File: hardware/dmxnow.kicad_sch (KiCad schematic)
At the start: 62 parts, among them J1 WAGO 2604-1102 (L N in), J2 DMX tail (1 GND 2 B 3 A), J3 PROG (3V3 GND D- D+ EN BOOT), J4 WAGO 2604-1102 (L_SW N out 1), J5 WAGO 2604-1102 (VLED_IN GND_L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, J6 WAGO 2604-1105 (VLED CH1-CH4), J7 WAGO 2604-1102 (L_SW N out 2,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, K1 G5RL-1A-E-HR DC5, Q1 AO3400A, Q2 AOD2610E, Q3 AOD2610E, Q4 AOD2610E, Q5 AOD2610E, SW1 PTS810 (BOOT/maintenance), U1 ESP32-C3-MINI-1-N4, U2 SP3485EN, U3 AP2112K-3.3, U4 74AHCT125

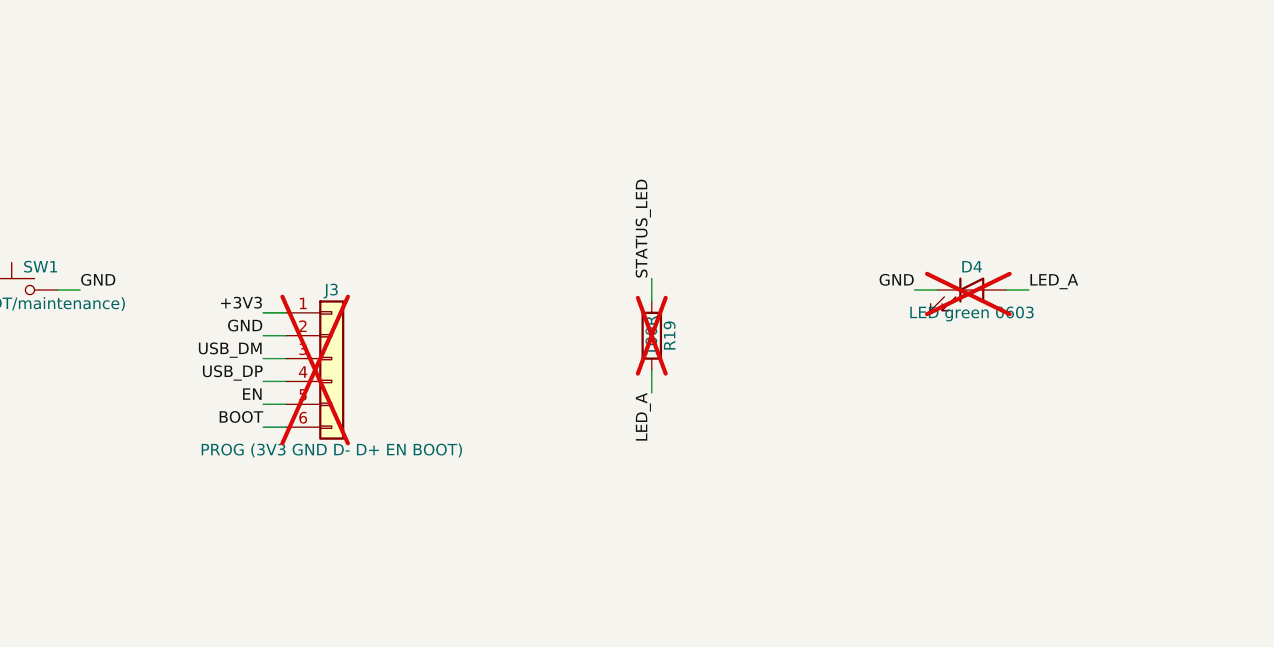
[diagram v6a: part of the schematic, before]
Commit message: hardware: cinquième passe de revue (J3 +5V, LED rouge, R15-R18, notes de commande)
- J3 passe à 7 pastilles : +5V (entrée de U3) pour programmer hors secteur sans
  réalimenter la sortie de l'AP2112K ; marquages 3V3 / 5V
- D4 LED rouge KT-0603R (C2286) + R19 330R : une LED verte VF 3,1 V ne s'allume pas
- R15-R18 décalées de 0,5 mm (4 mm sans composant de chaque côté de la découpe)
- marquages J2 en 1,0 mm ; références F1 / F2 ramenées sur la carte
- vias d'îlot : anneau entier dans les deux plans (plus de via à cheval sur un bord)
- SPEC : courant TX 350 mA, question J3-3V3 close, risque R-16 (OVP IRM-03 / AP2112K)
- README / REVIEW : 2 designs chez JLCPCB, remarque de commande complète, J6 arrêté chez WAGO

Co-Authored-By: Claude Opus 5.5 <noreply@anthropic.com>
Claude-Session: https://claude.ai/code/session_01B51M6ZY5abLxTmcevvc8Le
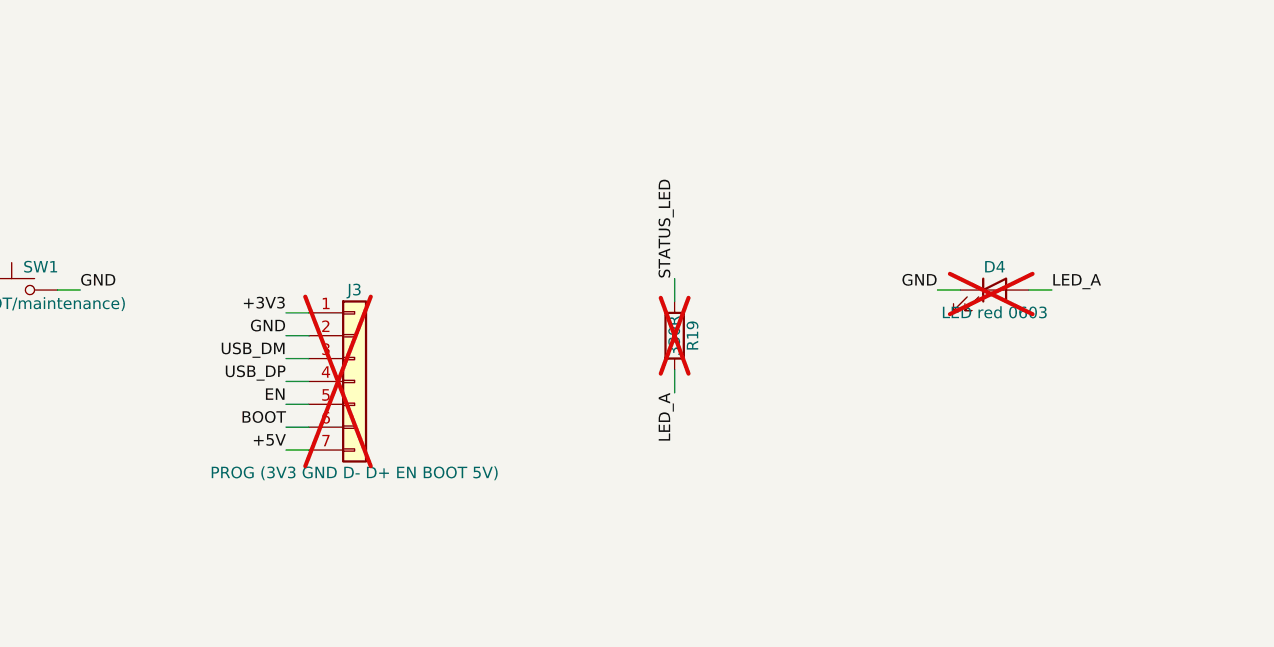
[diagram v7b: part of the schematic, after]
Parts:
- D4: value LED green 0603 -> LED red 0603; LCSC C12624 -> C2286; MPN KT-0603G -> KT-0603R
- J3: value PROG (3V3 GND D- D+ EN BOOT) -> PROG (3V3 GND D- D+ EN BOOT 5V); footprint Connector_PinHeader_2.54mm:PinHeader_1x06_P2.54mm_Vertical -> Connector_PinHeader_2.54mm:PinHeader_1x07_P2.54mm_Vertical; symbol Connector_Generic:Conn_01x06 -> Connector_Generic:Conn_01x07
- R19: value 100R -> 330R; LCSC C22775 -> C23138
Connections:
- net +5V: now also J3.7 (Pin_7)
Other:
- moved on the sheet: D4, R19
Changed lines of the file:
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@@
   )
   (symbol
-    (lib_id "Connector_Generic:Conn_01x06")
-    (at 325.12 147.32 0)
+    (lib_id "Connector_Generic:Conn_01x07")
+    (at 327.66 149.86 0)
     (unit 1)
     (in_bom yes)
@@
     (dnp yes)
     (property "Reference" "J3"
-      (at 325.12 139.7 0)
+      (at 327.66 139.7 0)
       (id 0)
       (effects
@@
       )
     )
-    (property "Value" "PROG (3V3 GND D- D+ EN BOOT)"
-      (at 325.12 157.48 0)
+    (property "Value" "PROG (3V3 GND D- D+ EN BOOT 5V)"
+      (at 327.66 160.02 0)
       (id 1)
       (effects
@@
       )
     )
-    (property "Footprint" "Connector_PinHeader_2.54mm:PinHeader_1x06_P2.54mm_Vertical"
-      (at 325.12 147.32 0)
+    (property "Footprint" "Connector_PinHeader_2.54mm:PinHeader_1x07_P2.54mm_Vertical"
+      (at 327.66 149.86 0)
       (id 2)
       (effects
@@
     )
     (property "Datasheet" ""
-      (at 325.12 147.32 0)
+      (at 327.66 149.86 0)
       (id 3)
       (effects
@@
     )
     (property "MPN" ""
-      (at 325.12 147.32 0)
+      (at 327.66 149.86 0)
       (id 4)
       (effects
@@
     )
     (property "LCSC" ""
-      (at 325.12 147.32 0)
+      (at 327.66 149.86 0)
       (id 5)
       (effects
@@
     )
     (property "Section" "main"
-      (at 325.12 147.32 0)
+      (at 327.66 149.86 0)
       (id 6)
       (effects
@@
     )
     (pin "6"
+    )
+    (pin "7"
     )
     (instances
@@
   (wire
     (pts
+      (xy 322.58 142.24)
       (xy 320.04 142.24)
-      (xy 317.5 142.24)
     )
     (stroke
@@
   )
   (label "+3V3"
-    (at 317.5 142.24 180)
-    (fields_autoplaced)
-    (effects
-      (font
-        (size 1.27 1.27)
-      )
-      (justify right bottom)
-    )
-  )
-  (wire
-    (pts
+    (at 320.04 142.24 180)
+    (fields_autoplaced)
+    (effects
+      (font
+        (size 1.27 1.27)
+      )
+      (justify right bottom)
+    )
+  )
+  (wire
+    (pts
+      (xy 322.58 144.78)
       (xy 320.04 144.78)
-      (xy 317.5 144.78)
     )
     (stroke
@@
   )
   (label "GND"
-    (at 317.5 144.78 180)
-    (fields_autoplaced)
-    (effects
-      (font
-        (size 1.27 1.27)
-      )
-      (justify right bottom)
-    )
-  )
-  (wire
-    (pts
+    (at 320.04 144.78 180)
+    (fields_autoplaced)
+    (effects
+      (font
+        (size 1.27 1.27)
+      )
+      (justify right bottom)
+    )
+  )
+  (wire
+    (pts
+      (xy 322.58 147.32)
       (xy 320.04 147.32)
-      (xy 317.5 147.32)
     )
     (stroke
@@
   )
   (label "USB_DM"
-    (at 317.5 147.32 180)
-    (fields_autoplaced)
-    (effects
-      (font
-        (size 1.27 1.27)
-      )
-      (justify right bottom)
-    )
-  )
-  (wire
-    (pts
+    (at 320.04 147.32 180)
+    (fields_autoplaced)
+    (effects
+      (font
+        (size 1.27 1.27)
+      )
+      (justify right bottom)
+    )
+  )
+  (wire
+    (pts
+      (xy 322.58 149.86)
       (xy 320.04 149.86)
-      (xy 317.5 149.86)
     )
     (stroke
@@
   )
   (label "USB_DP"
-    (at 317.5 149.86 180)
-    (fields_autoplaced)
-    (effects
-      (font
-        (size 1.27 1.27)
-      )
-      (justify right bottom)
-    )
-  )
-  (wire
-    (pts
+    (at 320.04 149.86 180)
+    (fields_autoplaced)
+    (effects
+      (font
+        (size 1.27 1.27)
+      )
+      (justify right bottom)
+    )
+  )
+  (wire
+    (pts
+      (xy 322.58 152.4)
       (xy 320.04 152.4)
-      (xy 317.5 152.4)
     )
     (stroke
@@
   )
   (label "EN"
-    (at 317.5 152.4 180)
-    (fields_autoplaced)
-    (effects
-      (font
-        (size 1.27 1.27)
-      )
-      (justify right bottom)
-    )
-  )
-  (wire
-    (pts
+    (at 320.04 152.4 180)
+    (fields_autoplaced)
+    (effects
+      (font
+        (size 1.27 1.27)
+      )
+      (justify right bottom)
+    )
+  )
+  (wire
+    (pts
+      (xy 322.58 154.94)
       (xy 320.04 154.94)
-      (xy 317.5 154.94)
     )
     (stroke
@@
   )
   (label "BOOT"
-    (at 317.5 154.94 180)
+    (at 320.04 154.94 180)
+    (fields_autoplaced)
+    (effects
+      (font
+        (size 1.27 1.27)
+      )
+      (justify right bottom)
+    )
+  )
+  (wire
+    (pts
+      (xy 322.58 157.48)
+      (xy 320.04 157.48)
+    )
+    (stroke
+      (width 0)
+      (type default)
+    )
+  )
+  (label "+5V"
+    (at 320.04 157.48 180)
     (fields_autoplaced)
     (effects
@@
   (symbol
     (lib_id "Device:R")
-    (at 360.68 144.78 0)
+    (at 363.22 144.78 0)
     (unit 1)
     (in_bom yes)
@@
     (dnp yes)
     (property "Reference" "R19"
-      (at 362.712 144.78 90)
+      (at 365.252 144.78 90)
       (id 0)
       (effects
@@
       )
     )
-    (property "Value" "100R"
-      (at 360.68 144.78 90)
+    (property "Value" "330R"
+      (at 363.22 144.78 90)
       (id 1)
       (effects
@@
     )
     (property "Footprint" "Resistor_SMD:R_0603_1608Metric"
-      (at 358.902 144.78 90)
+      (at 361.442 144.78 90)
       (id 2)
       (effects
@@
     )
     (property "Datasheet" ""
-      (at 360.68 144.78 0)
+      (at 363.22 144.78 0)
       (id 3)
       (effects
@@
     )
     (property "MPN" ""
-      (at 360.68 144.78 0)
+      (at 363.22 144.78 0)
       (id 4)
       (effects
@@
       )
     )
-    (property "LCSC" "C22775"
-      (at 360.68 144.78 0)
+    (property "LCSC" "C23138"
+      (at 363.22 144.78 0)
       (id 5)
       (effects
@@
     )
     (property "Section" "main"
-      (at 360.68 144.78 0)
+      (at 363.22 144.78 0)
       (id 6)
       (effects
@@
     )
     (property "Variant" "led"
-      (at 360.68 144.78 0)
+      (at 363.22 144.78 0)
       (id 7)
       (effects
@@
   (wire
     (pts
-      (xy 360.68 140.97)
-      (xy 360.68 138.43)
+      (xy 363.22 140.97)
+      (xy 363.22 138.43)
     )
     (stroke
@@
   )
   (label "STATUS_LED"
-    (at 360.68 138.43 90)
+    (at 363.22 138.43 90)
     (fields_autoplaced)
     (effects
@@
   (wire
     (pts
-      (xy 360.68 148.59)
-      (xy 360.68 151.13)
+      (xy 363.22 148.59)
+      (xy 363.22 151.13)
     )
     (stroke
@@
   )
   (label "LED_A"
-    (at 360.68 151.13 270)
+    (at 363.22 151.13 270)
     (fields_autoplaced)
     (effects
@@
   (symbol
     (lib_id "Device:LED")
-    (at 396.24 139.7 0)
+    (at 398.78 139.7 0)
     (unit 1)
     (in_bom yes)
@@
     (dnp yes)
     (property "Reference" "D4"
-      (at 396.24 137.16 0)
+      (at 398.78 137.16 0)
       (id 0)
       (effects
@@
       )
     )
-    (property "Value" "LED green 0603"
-      (at 396.24 142.24 0)
+    (property "Value" "LED red 0603"
+      (at 398.78 142.24 0)
       (id 1)
       (effects
@@
     )
     (property "Footprint" "LED_SMD:LED_0603_1608Metric"
-      (at 396.24 139.7 0)
+      (at 398.78 139.7 0)
       (id 2)
       (effects
@@
     )
     (property "Datasheet" ""
-      (at 396.24 139.7 0)
+      (at 398.78 139.7 0)
       (id 3)
       (effects
@@
       )
     )
-    (property "MPN" "KT-0603G"
-      (at 396.24 139.7 0)
+    (property "MPN" "KT-0603R"
+      (at 398.78 139.7 0)
       (id 4)
       (effects
@@
       )
     )
-    (property "LCSC" "C12624"
-      (at 396.24 139.7 0)
+    (property "LCSC" "C2286"
+      (at 398.78 139.7 0)
       (id 5)
       (effects
@@
     )
     (property "Section" "main"
-      (at 396.24 139.7 0)
+      (at 398.78 139.7 0)
       (id 6)
       (effects
@@
     )
     (property "Variant" "led"
-      (at 396.24 139.7 0)
+      (at 398.78 139.7 0)
       (id 7)
       (effects
@@
   (wire
     (pts
+      (xy 394.97 139.7)
       (xy 392.43 139.7)
-      (xy 389.89 139.7)
     )
     (stroke
@@
   )
   (label "GND"
-    (at 389.89 139.7 180)
-    (fields_autoplaced)
-    (effects
-      (font
-        (size 1.27 1.27)
-      )
-      (justify right bottom)
-    )
-  )
-  (wire
-    (pts
-      (xy 400.05 139.7)
+    (at 392.43 139.7 180)
+    (fields_autoplaced)
+    (effects
+      (font
+        (size 1.27 1.27)
+      )
+      (justify right bottom)
+    )
+  )
+  (wire
+    (pts
       (xy 402.59 139.7)
+      (xy 405.13 139.7)
     )
     (stroke
@@
   )
   (label "LED_A"
-    (at 402.59 139.7 0)
-    (fields_autoplaced)
-    (effects
+    (at 405.13 139.7 0)
+    (fields_autoplaced)
+    (effects

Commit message: hardware: J6 WAGO 2604-1105 (arrêté) remplacé par 2604-1102 + 2604-1103
Le 2604-1105 est « Discontinued » chez WAGO et à 0 chez JLCPCB. J6 devient
un 2604-1102 (VLED, CH1) et J8 un 2604-1103 (CH2-CH4), tous deux en stock et
de nouveau dans les fichiers d'assemblage JLCPCB.

- Blocs juxtaposés : 7,4 mm entre broches voisines d'après la fiche
  (L = (n - 1) x 5 + 7,4 mm) ; 8,0 mm au PCB (CH1 y 28,5 -> CH2 y 20,5).
  CH2-CH4 inchangés ; VLED et CH1 descendent de 3 mm.
- D3 passe à la verticale entre C7 et J6 ; C8 descend entre J6 et J5 ;
  plan VLED et pistes CH1 / GND_LED ajustés.
- SPEC, ADR 0008 (amendement), REVIEW, README : références, coût,
  remarque de commande.

Contrôles : netlist 0, PCB 0, DRC 0 erreur / 0 non connecté, canari OK.

Co-Authored-By: Claude Opus 5.5 <noreply@anthropic.com>
Claude-Session: https://claude.ai/code/session_01B51M6ZY5abLxTmcevvc8Le
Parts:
- added J8: WAGO 2604-1103 (CH2-CH4), dmxnow:TerminalBlock_WAGO_2604-1103_1x03_P5.00mm_Horizontal, symbol Connector:Screw_Terminal_01x03
- J6: value WAGO 2604-1105 (VLED CH1-CH4) -> WAGO 2604-1102 (VLED CH1); footprint dmxnow:TerminalBlock_WAGO_2604-1105_1x05_P5.00mm_Horizontal -> dmxnow:TerminalBlock_WAGO_2604-1102_1x02_P5.00mm_Horizontal; symbol Connector:Screw_Terminal_01x05 -> Connector:Screw_Terminal_01x02; LCSC C3818651 -> C3309286; MPN 2604-1105 -> 2604-1102
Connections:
- net CH2: now also J8.1 (Pin_1); no longer J6.3 (Pin_3)
- net CH3: now also J8.2 (Pin_2); no longer J6.4 (Pin_4)
- net CH4: now also J8.3 (Pin_3); no longer J6.5 (Pin_5)
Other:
- moved on the sheet: H1, H2, H3
